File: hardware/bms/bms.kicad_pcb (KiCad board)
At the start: 2 copper layers, 277 parts, among them J1 Screw_Terminal_01x01, J10 Conn_01x10, J11 USB_C_Receptacle_USB2.0, J12 Conn_01x03, J13 Conn_01x07, J2 Screw_Terminal_01x01, J3 Screw_Terminal_01x01, J4 Screw_Terminal_01x01, J5 Screw_Terminal_01x01, J6 Conn_01x02, J7 Conn_01x10, J8 Conn_01x02, J9 Conn_01x02, Q1 MMBT3904, Q2 Q_PMOS_GDS, Q3 Q_PMOS_GDS, Q4 BSZ018N04LS6ATMA1, Q5 IAUC120N04S6N006ATMA1, Q6 IAUC120N04S6N006ATMA1, Q7 BSZ018N04LS6ATMA1, Q8 BSZ018N04LS6ATMA1, Q9 BSZ018N04LS6ATMA1, SW1 SW_SPST, SW2 SW_Push, SW3 SW_Push, U1 BQ76952, U2 LM74700, U3 BQ24610, U4 LM5166X, U5 TPS62172DSG, U6 ESP32-C3-MINI-1-N4, U7 SN74LXC1T14DCKR, U8 USBLC6-2SC6

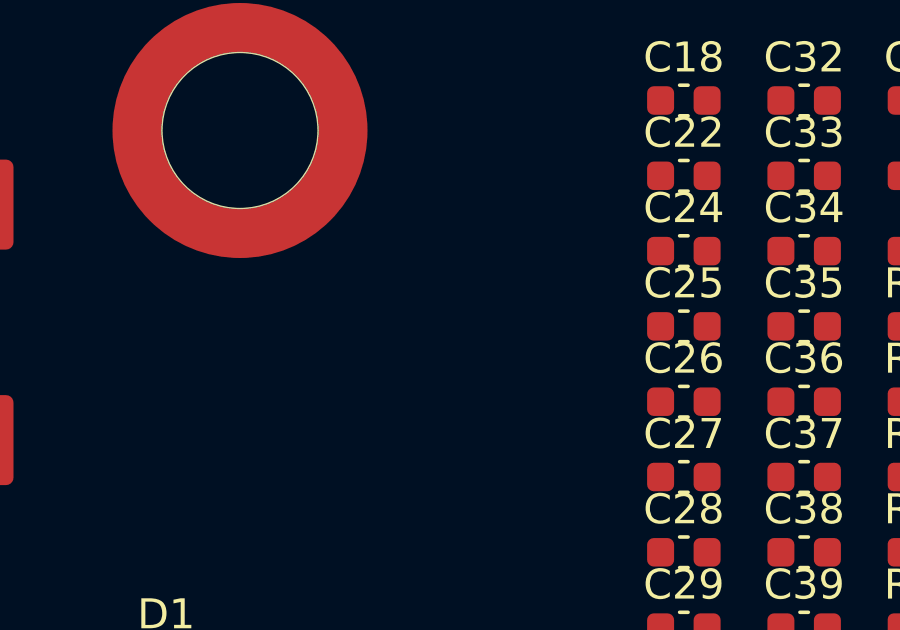
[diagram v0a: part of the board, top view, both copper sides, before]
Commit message: Sch cleanup, added extra netties
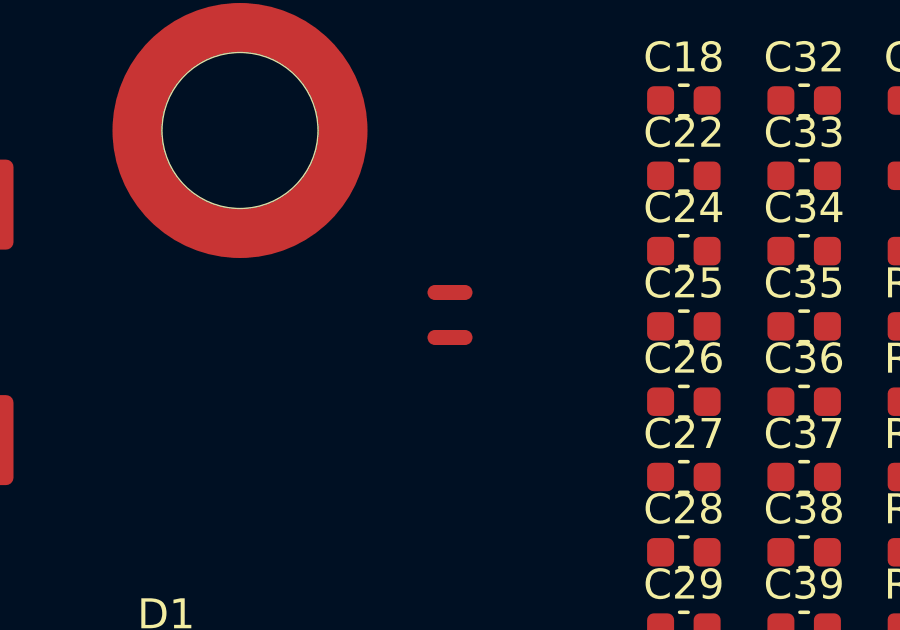
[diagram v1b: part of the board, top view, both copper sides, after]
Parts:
- added NT4: Net-Tie, NetTie:NetTie-2_SMD_Pad0.5mm, F.Cu at (66.7, 28.4)
- added NT5: Net-Tie, NetTie:NetTie-2_SMD_Pad0.5mm, F.Cu at (66.7, 29.9)
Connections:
- C52 pad 1: /BATTERY BALANCE AND MONITOR/VCHG+ -> /BATTERY CHARGER/SRN_CHG
- L1 pad 2: /BATTERY CHARGER/SRP_CHG -> Net-(L1-Pad2)
- R45 pad 2: /BATTERY CHARGER/SRP_CHG -> Net-(L1-Pad2)
- U3 pad 13: /BATTERY BALANCE AND MONITOR/VCHG+ -> /BATTERY CHARGER/SRN_CHG
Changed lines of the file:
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@@
   (net 165 "unconnected-(U6-NC-Pad34)")
   (net 166 "unconnected-(U6-NC-Pad35)")
+  (net 167 "/BATTERY CHARGER/SRN_CHG")
+  (net 168 "Net-(L1-Pad2)")
   (footprint "Connector_Molex:Molex_PicoBlade_53261-1071_1x10-1MP_P1.25mm_Horizontal" (layer "F.Cu")
     (at 48.485 49.05)
@@
     )
   )
+  (footprint "NetTie:NetTie-2_SMD_Pad0.5mm" (layer "F.Cu")
+    (at 66.7 28.4)
+    (descr "Net tie, 2 pin, 0.5mm square SMD pads")
+    (tags "net tie")
+    (property "Sheetfile" "charger.kicad_sch")
+    (property "Sheetname" "BATTERY CHARGER")
+    (attr exclude_from_pos_files allow_missing_courtyard)
+    (net_tie_pad_groups "1, 2")
+    (fp_text reference "NT4" (at 0 -1.2) (layer "F.SilkS") hide
+        (effects (font (size 1 1) (thickness 0.15)))
+    )
+    (fp_text value "Net-Tie" (at 0 1.2) (layer "F.Fab") hide
+        (effects (font (size 1 1) (thickness 0.15)))
+    )
+    (fp_poly
+      (pts
+        (xy -0.5 -0.25)
+        (xy 0.5 -0.25)
+        (xy 0.5 0.25)
+        (xy -0.5 0.25)
+      )
+      (stroke (width 0) (type solid)) (fill solid) (layer "F.Cu"))
+    (pad "1" smd circle (at -0.5 0) (size 0.5 0.5) (layers "F.Cu")
+      (net 168 "Net-(L1-Pad2)") (pinfunction "1") (pintype "passive"))
+    (pad "2" smd circle (at 0.5 0) (size 0.5 0.5) (layers "F.Cu")
+      (net 39 "/BATTERY CHARGER/SRP_CHG") (pinfunction "2") (pintype "passive"))
+  )
   (footprint "Capacitor_SMD:C_0603_1608Metric" (layer "F.Cu")
     (at 74.495 27.02)
@@
       (stroke (width 0.1) (type solid)) (layer "F.Fab"))
     (pad "1" smd roundrect (at -0.775 0) (size 0.9 0.95) (layers "F.Cu" "F.Paste" "F.Mask") (roundrect_rratio 0.25)
-      (net 3 "/BATTERY BALANCE AND MONITOR/VCHG+") (pintype "passive"))
+      (net 167 "/BATTERY CHARGER/SRN_CHG") (pintype "passive"))
     (pad "2" smd roundrect (at 0.775 0) (size 0.9 0.95) (layers "F.Cu" "F.Paste" "F.Mask") (roundrect_rratio 0.25)
       (net 39 "/BATTERY CHARGER/SRP_CHG") (pintype "passive"))
@@
       (net 42 "/BATTERY CHARGER/VFB") (pinfunction "VFB") (pintype "input"))
     (pad "13" smd roundrect (at 1.9875 1.25) (size 0.775 0.25) (layers "F.Cu" "F.Paste" "F.Mask") (roundrect_rratio 0.25)
-      (net 3 "/BATTERY BALANCE AND MONITOR/VCHG+") (pinfunction "SRN") (pintype "input"))
+      (net 167 "/BATTERY CHARGER/SRN_CHG") (pinfunction "SRN") (pintype "input"))
     (pad "14" smd roundrect (at 1.9875 0.75) (size 0.775 0.25) (layers "F.Cu" "F.Paste" "F.Mask") (roundrect_rratio 0.25)
       (net 39 "/BATTERY CHARGER/SRP_CHG") (pinfunction "SRP") (pintype "input"))
@@
       (net 37 "/BATTERY CHARGER/SW_NODE") (pinfunction "1") (pintype "passive") (thermal_bridge_angle 45))
     (pad "2" smd roundrect (at 5.475 0 180) (size 3.25 4.9) (layers "F.Cu" "F.Paste" "F.Mask") (roundrect_rratio 0.25)
-      (net 39 "/BATTERY CHARGER/SRP_CHG") (pinfunction "2") (pintype "passive") (thermal_bridge_angle 45))
+      (net 168 "Net-(L1-Pad2)") (pinfunction "2") (pintype "passive") (thermal_bridge_angle 45))
     (model "./3d_models/HCM1307-R.STEP"
       (offset (xyz 0 0 0))
@@
     )
   )
+  (footprint "NetTie:NetTie-2_SMD_Pad0.5mm" (layer "F.Cu")
+    (at 66.7 29.9)
+    (descr "Net tie, 2 pin, 0.5mm square SMD pads")
+    (tags "net tie")
+    (property "Sheetfile" "charger.kicad_sch")
+    (property "Sheetname" "BATTERY CHARGER")
+    (attr exclude_from_pos_files allow_missing_courtyard)
+    (net_tie_pad_groups "1, 2")
+    (fp_text reference "NT5" (at 0 -1.2) (layer "F.SilkS") hide
+        (effects (font (size 1 1) (thickness 0.15)))
+    )
+    (fp_text value "Net-Tie" (at 0 1.2) (layer "F.Fab") hide
+        (effects (font (size 1 1) (thickness 0.15)))
+    )
+    (fp_poly
+      (pts
+        (xy -0.5 -0.25)
+        (xy 0.5 -0.25)
+        (xy 0.5 0.25)
+        (xy -0.5 0.25)
+      )
+      (stroke (width 0) (type solid)) (fill solid) (layer "F.Cu"))
+    (pad "1" smd circle (at -0.5 0) (size 0.5 0.5) (layers "F.Cu")
+      (net 3 "/BATTERY BALANCE AND MONITOR/VCHG+") (pinfunction "1") (pintype "passive"))
+    (pad "2" smd circle (at 0.5 0) (size 0.5 0.5) (layers "F.Cu")
+      (net 167 "/BATTERY CHARGER/SRN_CHG") (pinfunction "2") (pintype "passive"))
+  )
   (footprint "TestPoint:TestPoint_Pad_D1.0mm" (layer "F.Cu")
     (at 83.165 53.47)
@@
       (net 3 "/BATTERY BALANCE AND MONITOR/VCHG+") (pintype "passive"))
     (pad "2" smd roundrect (at 2.9625 0) (size 1.225 3.35) (layers "F.Cu" "F.Paste" "F.Mask") (roundrect_rratio 0.204082)
-      (net 39 "/BATTERY CHARGER/SRP_CHG") (pintype "passive"))
+      (net 168 "Net-(L1-Pad2)") (pintype "passive"))
     (model "${KICAD6_3DMODEL_DIR}/Resistor_SMD.3dshapes/R_2512_6332Metric.wrl"
       (offset (xyz 0 0 0))

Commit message: Continued layout, defined board area based on mech assembly
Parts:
- removed J9: Conn_01x02, Connector_Molex:Molex_PicoBlade_53261-0271_1x02-1MP_P1.25mm_Horizontal
- removed NT3: Net-Tie, NetTie:NetTie-2_SMD_Pad2.0mm
- removed R72: 0R, Resistor_SMD:R_0603_1608Metric
- added TP65: TestPoint, TestPoint:TestPoint_Pad_D1.0mm, F.Cu at (280.2, 126.0)
- L1: footprint bms:HCM1307-3R3-R -> bms:IND_ETQP5M3R3YFK
- R20, R21, R32, R33, R35, R36, R37: footprint Resistor_SMD:R_1210_3225Metric -> Resistor_SMD:R_0805_2012Metric
- moved C16 202.9 mm to (301.1, 66.8)
- moved C37 202.9 mm to (279.2, 64.1)
- moved C8 202.9 mm to (241.2, 66.8)
- moved D11 202.9 mm to (254.5, 128.2)
- moved D15 202.9 mm to (303.2, 130.2)
- moved R12 202.9 mm to (283.2, 64.1)
- moved R60 202.9 mm to (279.2, 102.5)
- moved R63 202.9 mm to (279.2, 110.0)
- moved R66 202.9 mm to (279.2, 117.5)
- moved R68 202.9 mm to (283.2, 102.5)
- moved R71 202.9 mm to (283.2, 110.0)
- moved R74 202.9 mm to (283.2, 117.5)
- moved TP55 202.9 mm to (256.9, 114.9)
- moved TP56 202.9 mm to (256.9, 118.0)
- moved TP57 202.9 mm to (274.7, 120.3)
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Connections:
- net /MCU/PWM_OUT1 renamed /MCU/PWM_OUT
- J13 pad 1: /V_CELLS_0 -> /V_CELLS_6
- J13 pad 2: /V_CELLS_1 -> /V_CELLS_5
- J13 pad 3: /V_CELLS_2 -> /V_CELLS_4
- J13 pad 5: /V_CELLS_4 -> /V_CELLS_2
- J13 pad 6: /V_CELLS_5 -> /V_CELLS_1
- J13 pad 7: /V_CELLS_6 -> /V_CELLS_0
- J3 pad 1: /BATTERY BALANCE AND MONITOR/VBAT- -> GND
- NT1 pad 2: /BATTERY BALANCE AND MONITOR/VBAT- -> GND
- R40 pad 2: /BATTERY BALANCE AND MONITOR/VBAT- -> GND
- R65 pad 1: /MCU/GPIO7 -> /CHG_STAT1
- R65 pad 2: /CHG_STAT2 -> /MCU/GPIO5
- R74 pad 1: /CHG_STAT1 -> /CHG_STAT2
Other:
- board outline added: 120 x 45 mm
- copper layers 2 -> 4

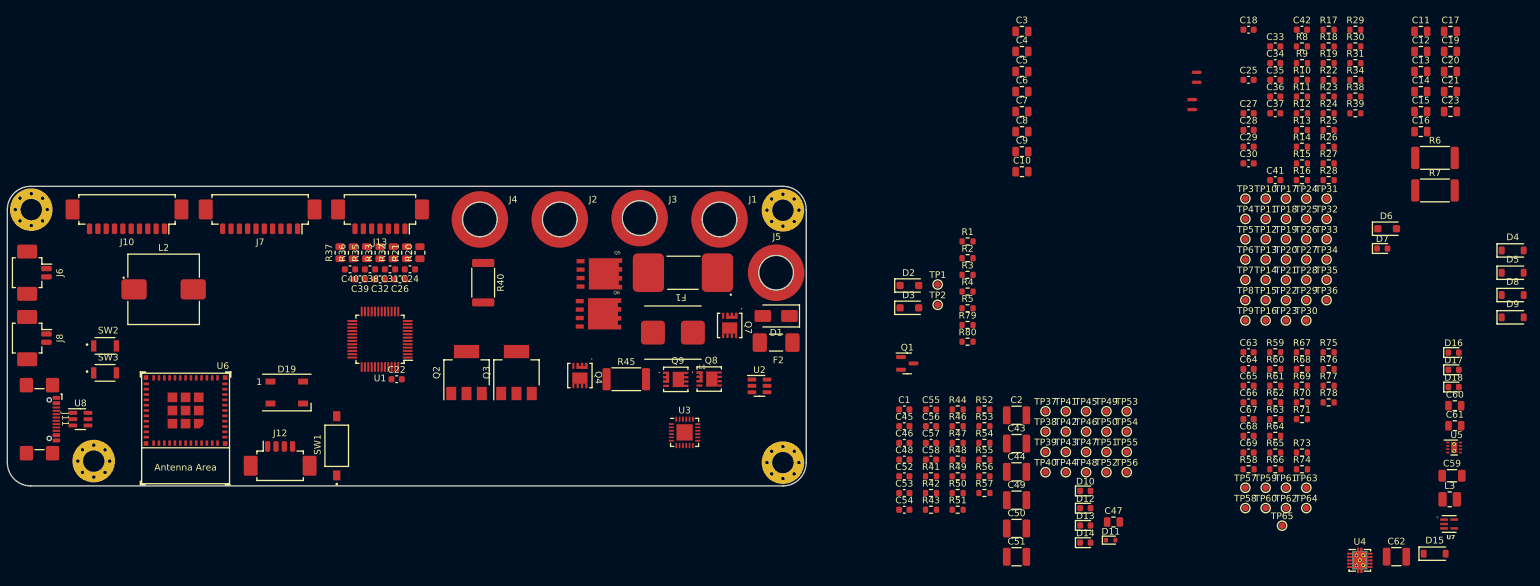
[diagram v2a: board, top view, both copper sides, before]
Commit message: Updated test points to 0.5mm to save space, continued layout
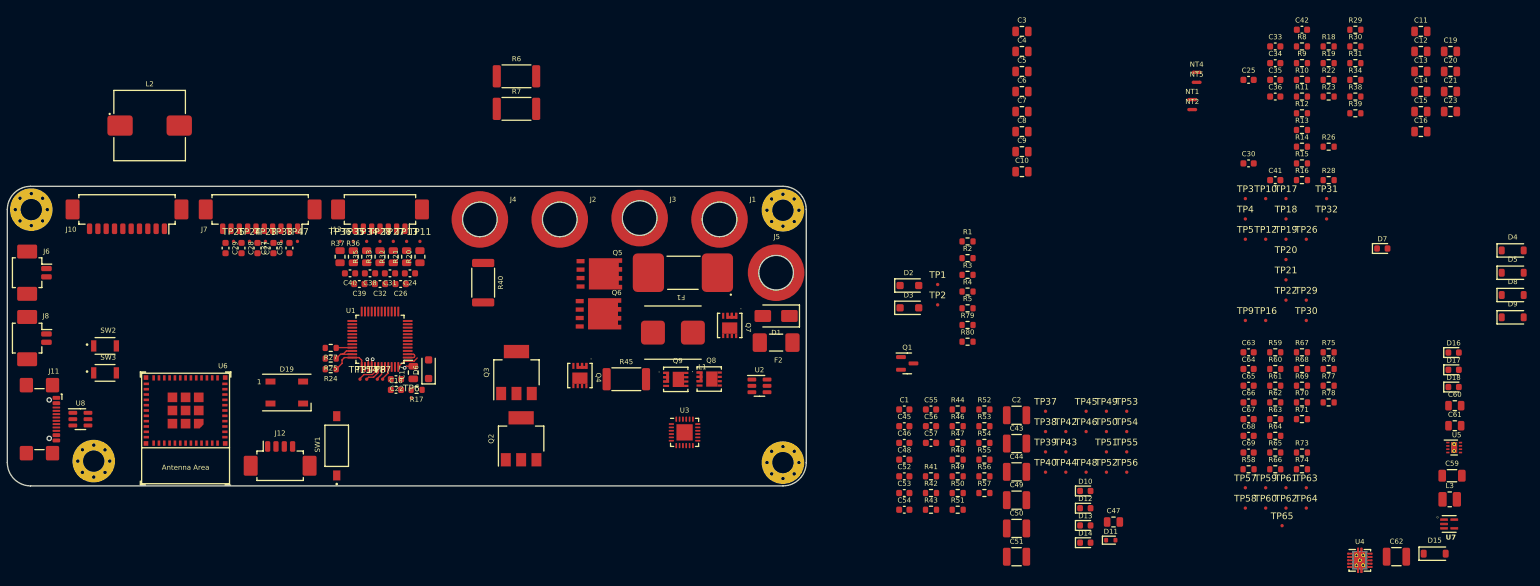
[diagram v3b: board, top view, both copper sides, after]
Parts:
- removed TP41: TestPoint, TestPoint:TestPoint_Pad_D1.0mm
- TP1, TP10, TP11, TP12, TP13, TP14, TP15, TP16, TP17, TP18, TP19, TP2, TP20, TP21, TP22, TP23, TP24, TP25, TP26, TP27, TP28, TP29, TP3, TP30, TP31, TP32, TP33, TP34, TP35, TP36, TP37, TP38, TP39, TP4, TP40, TP42, TP43, TP44, TP45, TP46, TP47, TP48, TP49, TP5, TP50, TP51, TP52, TP53, TP54, TP55, TP56, TP57, TP58, TP59, TP6, TP60, TP61, TP62, TP63, TP64, TP65, TP7, TP8, TP9: footprint TestPoint:TestPoint_Pad_D1.0mm -> bms:TestPoint_Pad_D0.5mm
- moved C17 164.0 mm to (149.8, 103.0), turned to 90 degrees
- moved TP25 161.2 mm to (122.8, 83.3)
- moved TP24 158.9 mm to (125.2, 83.3)
- moved TP33 157.0 mm to (129.9, 83.3)
- moved R24 154.7 mm to (137.3, 102.5), turned to 180 degrees
- moved C29 154.4 mm to (121.5, 84.3), turned to -90 degrees
- moved R25 153.8 mm to (137.3, 100.9), turned to 180 degrees
- moved TP23 153.7 mm to (127.5, 83.3)
- moved R27 152.4 mm to (137.3, 99.3), turned to 180 degrees
- moved C28 152.3 mm to (124.0, 84.3), turned to -90 degrees
- moved C37 151.8 mm to (128.8, 84.3), turned to 90 degrees
- moved C27 150.2 mm to (126.3, 84.3), turned to -90 degrees
- moved TP36 148.4 mm to (138.8, 83.3)
- moved R17 147.3 mm to (150.2, 105.6), turned to 180 degrees
- moved TP35 146.3 mm to (140.8, 83.3)
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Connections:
- C37 pad 1: /BATTERY BALANCE AND MONITOR/THERM_8 -> /THERM_0
- TP33 pad 1: /BATTERY BALANCE AND MONITOR/THERM_8 -> /THERM_0
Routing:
- net Net-(U1-BREG): track 0.00 -> 6.04 mm
- net Net-(U1-REG1): track 0.00 -> 4.43 mm
- net /BATTERY BALANCE AND MONITOR/LD: track 0.00 -> 3.50 mm
- net /BATTERY BALANCE AND MONITOR/VC16: track 0.00 -> 3.41 mm
- net /BATTERY BALANCE AND MONITOR/PACK: track 0.00 -> 3.00 mm
- net /BATTERY BALANCE AND MONITOR/RST_SHUT: track 0.00 -> 2.43 mm
- net /BATTERY BALANCE AND MONITOR/VC15: track 0.00 -> 2.40 mm
- net /BATTERY BALANCE AND MONITOR/CHG: track 0.00 -> 2.19 mm
- net /BATTERY BALANCE AND MONITOR/DSG: track 0.00 -> 2.11 mm
- net GND: track 0.00 -> 1.40 mm, vias 0 -> 1
- net /BATTERY BALANCE AND MONITOR/PDSG: track 0.00 -> 1.22 mm, vias 0 -> 1
- net /BATTERY BALANCE AND MONITOR/PCHG: track 0.00 -> 1.22 mm, vias 0 -> 1

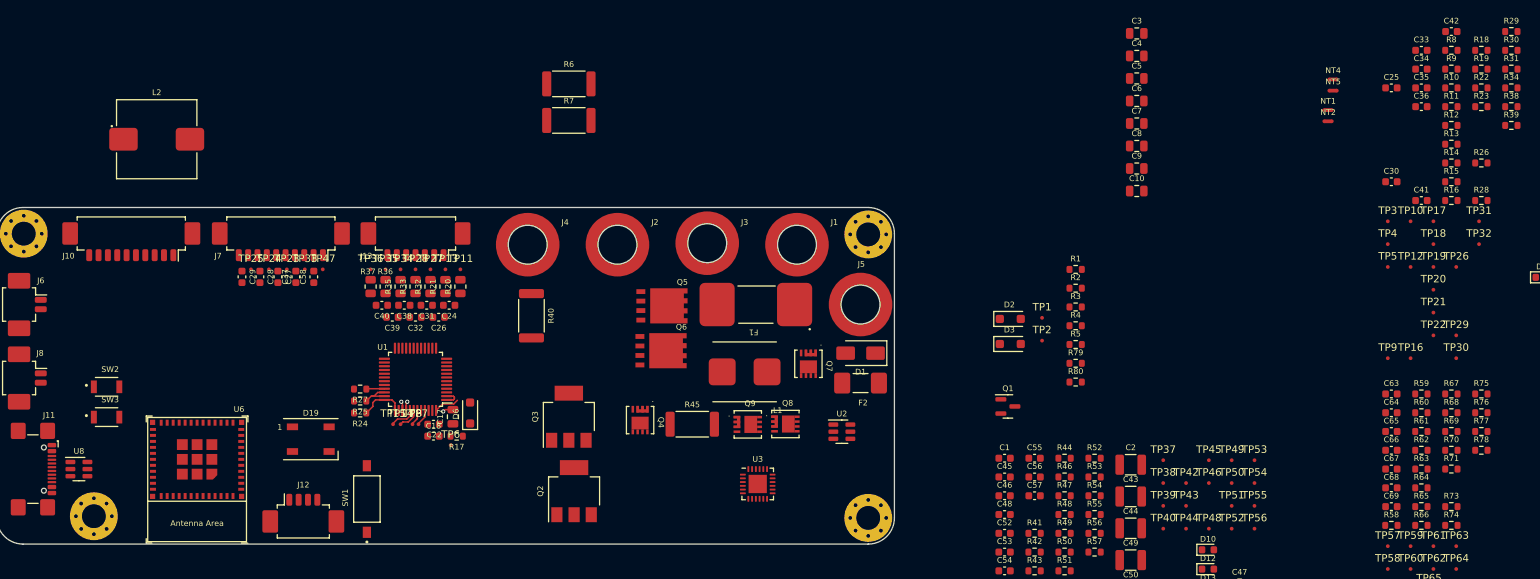
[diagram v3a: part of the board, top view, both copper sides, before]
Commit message: Simplified chassis connection, only at one mounting hole and left other holes NC (no chassis plane on PCB
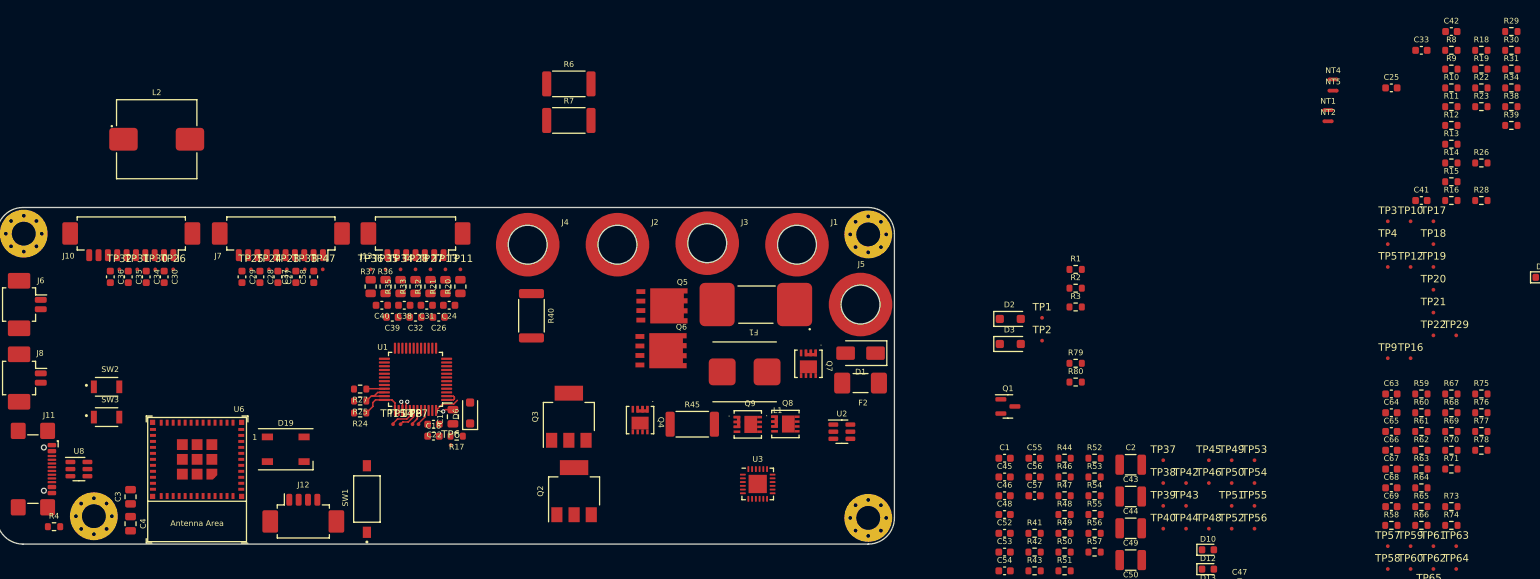
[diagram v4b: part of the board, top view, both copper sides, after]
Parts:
- removed C10, C5, C6, C7, C8, C9: 0.1uF, Capacitor_SMD:C_0805_2012Metric
- removed R5: 10M, Resistor_SMD:R_0603_1608Metric
- moved TP32 181.8 mm to (105.2, 83.3)
- moved TP31 179.5 mm to (107.5, 83.3)
- moved C36 176.7 mm to (104.0, 84.3), turned to -90 degrees
- moved C35 174.7 mm to (106.3, 84.3), turned to -90 degrees
- moved TP30 174.3 mm to (110.0, 83.3)
- moved C34 172.7 mm to (108.8, 84.3), turned to -90 degrees
- moved TP26 171.5 mm to (112.3, 83.3)
- moved C30 164.6 mm to (111.2, 84.3), turned to -90 degrees
- moved C4 148.3 mm to (106.7, 117.3), turned to -90 degrees
- moved C3 148.1 mm to (106.7, 113.7), turned to 90 degrees
- moved R4 139.2 mm to (96.4, 117.7)
- moved D19 3.61 mm to (127.4, 107.3)
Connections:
- H2 pad 1: GNDPWR -> unconnected-(H2-Pad1)
- H3 pad 1: GNDPWR -> unconnected-(H3-Pad1)
- H4 pad 1: GNDPWR -> unconnected-(H4-Pad1)

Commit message: Some routing for thermistors and cell taps to see if it works
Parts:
- moved D9 181.0 mm to (134.2, 85.2), turned to 90 degrees
- moved R29 180.3 mm to (117.8, 100.8), turned to 90 degrees
- moved D8 178.4 mm to (136.6, 85.2), turned to 90 degrees
- moved R28 166.5 mm to (123.0, 100.8), turned to 90 degrees
- moved TP19 161.0 mm to (119.8, 83.3)
- moved R66 160.5 mm to (119.5, 100.8), turned to -90 degrees
- moved R30 160.0 mm to (137.3, 97.8), turned to 180 degrees
- moved R31 158.9 mm to (137.3, 96.2), turned to 180 degrees
- moved R64 158.4 mm to (121.2, 100.8), turned to -90 degrees
- moved R34 155.0 mm to (139.9, 92.9), turned to 180 degrees
- moved R26 150.3 mm to (143.2, 112.3)
- moved TP21 145.9 mm to (135.2, 97.8)
- moved TP20 145.9 mm to (135.2, 94.7)
- moved TP22 145.7 mm to (135.2, 96.2)
- moved C25 139.8 mm to (139.9, 94.5), turned to 180 degrees
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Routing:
- net GND: track 1.40 -> 69.3 mm, vias 1 -> 46
- net /THERM_7: track 0.00 -> 47.1 mm
- net /THERM_6: track 0.00 -> 44.5 mm
- net /THERM_5: track 0.00 -> 41.8 mm
- net /THERM_4: track 0.00 -> 39.3 mm
- net /THERM_3: track 0.00 -> 29.7 mm
- net /THERM_2: track 0.00 -> 25.9 mm
- net /THERM_1: track 0.00 -> 25.4 mm
- net /BATTERY BALANCE AND MONITOR/VC15: track 2.40 -> 27.5 mm
- net /THERM_0: track 0.00 -> 24.8 mm
- net /BATTERY BALANCE AND MONITOR/VC0: track 0.00 -> 17.7 mm
- net /BATTERY BALANCE AND MONITOR/VC16: track 3.41 -> 18.4 mm
- net /BATTERY BALANCE AND MONITOR/VC1: track 0.00 -> 11.8 mm
- net /BATTERY BALANCE AND MONITOR/VC4: track 0.00 -> 11.1 mm
- net /BATTERY BALANCE AND MONITOR/VC2: track 0.00 -> 10.6 mm
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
